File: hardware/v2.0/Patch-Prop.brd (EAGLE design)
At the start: 100 x 80 mm, 51 parts, among them IC1 TPS77033, IC2 ATMEGA168, IC3 XBEE, IC4 MMA8452Q, U1 MCP73831, U2 MCP1253, X1 USBSMD

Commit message: Tweaking naming and notes
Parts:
- removed R9: 470, SparkFun:0402-RES
- removed U1: MCP73831, SparkFun:SOT23-5
- added IC5: MCP1253, CH_Microchip:MSOP8
- added R7: 10k, rcl:R0603
- C1, C5: device rcl:C0603 -> CH_passive:0603
- C10, C9: value 4.7uF -> 0.1uF; device SparkFun:0402-CAP -> rcl:C0603
- C11: value 0.1uF -> 4.7uF
- C12: value 1uF -> .1uF; device CH_passive:0603 -> rcl:C0603
- C13: device CH_passive:0603 -> rcl:C0603
- C14: value 10uF -> .1uF; device CH_passive:0603 -> rcl:C0603
- C3: value .1uF -> 1uF
- C4: value .1uF -> 10uF; device rcl:C0603 -> CH_passive:0603
- C7: value 0.1uF -> 4.7uF; device rcl:C0603 -> SparkFun:0402-CAP
- C8: device rcl:C0603 -> SparkFun:0402-CAP
- IC2: value ATMEGA168 -> XBEE; device SparkFun:TQFP32-08 -> adafruit:XBEE
- IC3: value XBEE -> MMA8452Q; device adafruit:XBEE -> eski-ic:QFN-16
- IC4: value MMA8452Q -> ATMEGA168; device eski-ic:QFN-16 -> SparkFun:TQFP32-08
- JP2: device SparkFun-Connectors:JST-3-SMD -> SparkFun-Connectors:JST-2-SMD
- JP3: device SparkFun-Connectors:JST-2-SMD -> SparkFun-Connectors:1X02
- JP5: device SparkFun-Connectors:JST-2-SMD -> SparkFun-Connectors:JST-3-SMD
- JP7: device SparkFun-Connectors:1X02 -> SparkFun-Connectors:JST-2-SMD
- R2: value 10k -> 470; device rcl:R0603 -> SparkFun:0402-RES
- R3: value 470 -> 10k
- R4: value 10k -> 2K; device rcl:R0603 -> SparkFun:0402-RES
- R5: value 2K -> 470; device SparkFun:0402-RES -> rcl:R0603
- U2: value MCP1253 -> MCP73831; device CH_Microchip:MSOP8 -> SparkFun:SOT23-5
- moved C9 88.7 mm to (5.08, 15.2)
- moved U2 85.2 mm to (87.6, 34.3)
- moved C8 83.2 mm to (87.6, 30.5)
- moved C7 81.6 mm to (91.4, 35.6)
- moved C10 77.5 mm to (10.2, 27.9)
- moved JP3 71.5 mm to (67.3, 16.5)
- moved JP5 56.2 mm to (15.2, 77.5)
- moved C1 52.4 mm to (22.9, 33.0)
- moved JP6 48.5 mm to (19.1, 11.4)
- moved R2 44.6 mm to (87.6, 26.7)
- moved IC3 44.4 mm to (5.08, 26.7)
- moved R4 42.6 mm to (91.4, 30.5)
- moved C13 42.4 mm to (59.7, 59.7)
- moved C5 39.6 mm to (30.5, 33.0)
- moved IC4 37.8 mm to (17.8, 62.2)
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- renumbered D4 to D1, LED7 to LED1, R12 to R6, U$1 to IC6
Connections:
- net +3V3: now also C13.1, C14.1, C4.2, C9.1, IC2.1, IC3.PIN1, IC3.PIN14, IC4.18, IC4.4, IC4.6, IC5.3, IC5.7, R5.2, R7.2; no longer C13.2, C5.1, C6.1, C8.1, IC2.18, IC2.4, IC2.6, IC3.1, IC4.PIN1, IC4.PIN14, R3.2, R4.2, U2.3, U2.7
- net +5V: now also JP5.3; no longer JP2.3
- net BLUE: now also IC4.14; no longer IC2.14
- net DTR: now also C12.1; no longer C4.1
- net GND: now also C13.2, C14.2, C3.2, C4.1, C5.1, IC2.10, IC3.PIN10, IC3.PIN12, IC3.PIN5, IC3.PIN7, IC4.21, IC4.3, IC4.5, IC5.4, IC5.8, JP2.1, JP5.2, R3.1, R4.2, U2.2; no longer C1.2, C13.1, C14.1, C5.2, C6.2, IC2.21, IC2.3, IC2.5, IC3.10, IC4.PIN10, IC4.PIN12, IC4.PIN5, IC4.PIN7, JP2.2, JP6.1, R2.1, R5.2, U1.2, U2.4, U2.8
- net GREEN: now also IC4.9; no longer IC2.9
- net INT0: now also IC4.32; no longer IC2.32
- net INT1: now also IC3.PIN11, IC4.1; no longer IC2.1, IC4.PIN11
- net INT2: now also IC3.PIN9; no longer IC4.PIN9
- net MISO: now also IC4.16; no longer IC2.16
- net MOSI: now also IC4.15; no longer IC2.15
- net N$1: now also C6.1, IC2.17, SJ2.2; no longer C3.1, IC3.17, SJ1.2
- net N$10: now also C5.2, IC5.2; no longer C14.2, U2.2
- net N$11: now also R4.1, U2.5; no longer R5.1, U1.5
- net N$14: now also R2.1, U2.1; no longer R9.1, U1.1
- net N$16: now also C10.1, IC3.PIN2; no longer C7.1, IC4.PIN2
- net N$18: now also IC2.12, SJ2.1; no longer IC3.12, SJ1.1
- net N$19: now also IC2.5, SJ1.1; no longer IC3.5, SJ2.1
- net N$2: now also C6.2, R3.2; no longer C3.2, R2.2
- net N$5: now also R5.1; no longer R3.1
- net N$6: now also C1.1, IC5.5; no longer C12.1, U2.5
- net N$7: now also C1.2, IC5.6; no longer C12.2, U2.6
- net N$8: now also R2.2; no longer R9.2
- net PGOOD: now also IC5.1; no longer U2.1
- net PROXIN: now also IC4.23, JP5.1; no longer IC2.23, JP2.1
- net RED: now also IC4.13; no longer IC2.13
- net RESET: now also C12.2, IC4.29, R7.1, SJ1.2; no longer C4.2, IC2.29, R4.1, SJ2.2
- net RXD: now also IC2.2, IC4.30; no longer IC2.30, IC3.2
- net SCK: now also IC4.17; no longer IC2.17
- net SCL: now also IC3.PIN4, IC4.28; no longer IC2.28, IC4.PIN4
- net SDA: now also IC3.PIN6, IC4.27; no longer IC2.27, IC4.PIN6
- net STATUS: now also IC4.11; no longer IC2.11
- net TXD: now also IC2.3, IC4.31; no longer IC2.31, IC3.3
- net USB_VIN: now also C7.1, JP3.2, U2.4; no longer C9.1, JP6.2, U1.4
- net V+: now also C3.1, C8.1, JP2.2, JP6.1, JP7.2, U2.3; no longer C1.1, C10.1, JP3.2, JP5.2, JP7.1, U1.3
- net VIBE: now also JP6.2, JP7.1; no longer JP5.1, JP7.2
- net VIBE_CONTROL: now also IC4.12; no longer IC2.12

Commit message: Working on PCB
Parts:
- removed C7, C8: 4.7uF, SparkFun:0402-CAP
- removed JP3: (no value), SparkFun-Connectors:1X02
- added C15, C16: 4.7uF, rcl:C0603
- C1, C4, C5: device CH_passive:0603 -> rcl:C0603
- D1: value Yellow -> (none); device SparkFun:LED-0603 -> led:CHIPLED_0805
- R1: device CH_passive:0603 -> rcl:R0603
- R2: device SparkFun:0402-RES -> rcl:R0603
- R4: value 2K -> 2k; device SparkFun:0402-RES -> rcl:R0603
- moved R2 88.8 mm to (8.00, 66.0)
- moved X1 88.0 mm to (6.50, 42.0), turned to 180 degrees
- moved D1 87.5 mm to (11.0, 61.0)
- moved R4 87.0 mm to (12.0, 66.0)
- moved T2 86.6 mm to (12.0, 15.0)
- moved U2 85.3 mm to (7.00, 62.0)
- moved IC6 73.1 mm to (93.0, 14.0)
- moved JP5 68.0 mm to (83.0, 72.0), turned to 90 degrees
- moved IC5 67.8 mm to (74.0, 4.00)
- moved C1 66.8 mm to (83.0, 4.00), turned to 90 degrees
- moved L1 63.5 mm to (86.0, 4.00), turned to 90 degrees
- moved C3 62.2 mm to (59.0, 4.00), turned to 90 degrees
- moved JP1 59.6 mm to (11.0, 41.0), turned to 90 degrees
- moved R7 58.6 mm to (37.0, 30.0)
- moved C2 56.8 mm to (55.0, 4.00), turned to 90 degrees
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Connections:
- net +3V3: now also C4.1; no longer C4.2
- net GND: now also C15.2, C16.2, C4.2, C5.2; no longer C4.1, C5.1, C7.2, C8.2, JP3.1
- net N$10: now also C5.1, R1.1; no longer C5.2, R1.2
- net PGOOD: now also R1.2; no longer R1.1
- net USB_VIN: now also C16.1; no longer C7.1, JP3.2
- net V+: now also C15.1; no longer C8.1
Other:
- board size 100 x 80 mm -> 45 x 45 mm

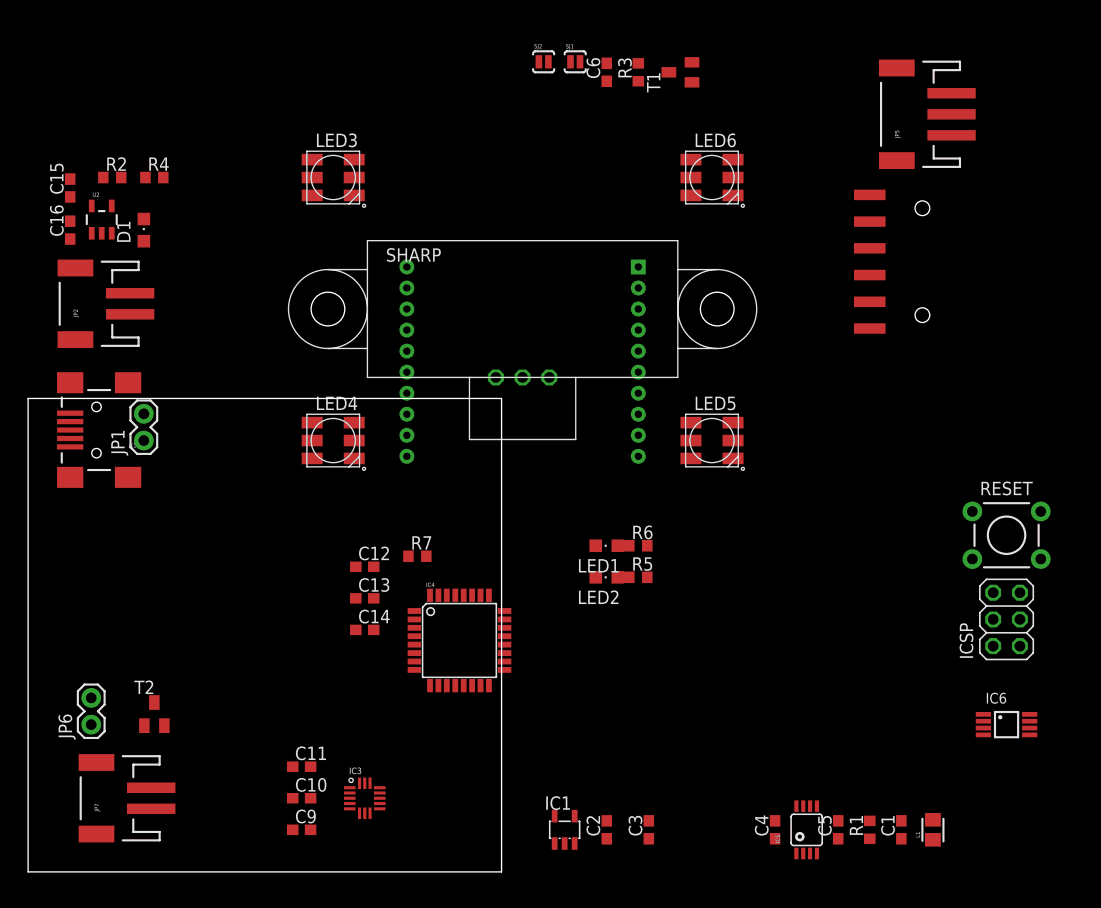
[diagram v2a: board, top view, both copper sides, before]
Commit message: Tentative part layout for propinquity board
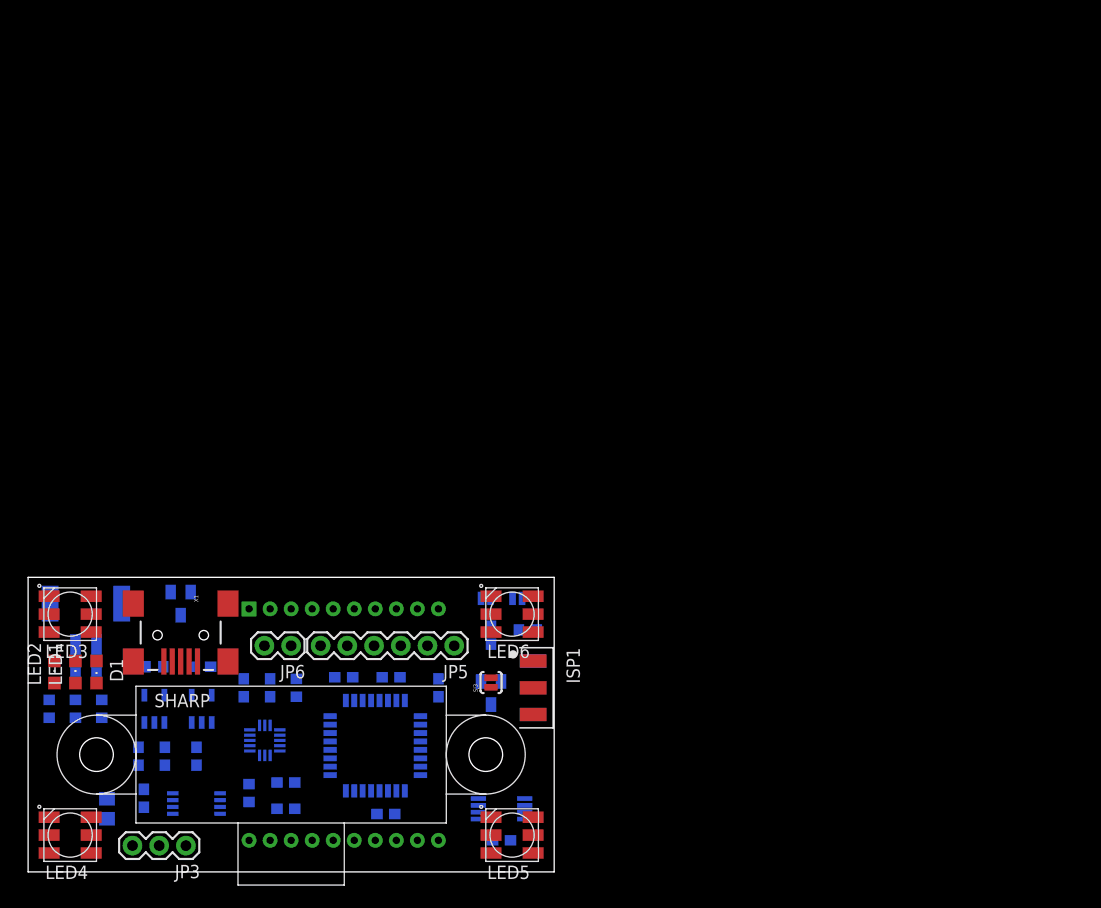
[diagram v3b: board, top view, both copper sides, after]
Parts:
- removed ICSP: (no value), pinhead:2X03
- removed JP1: (no value), SparkFun-Connectors:1X02
- removed JP4: (no value), SparkFun:1X06-SMD
- removed JP7: (no value), SparkFun-Connectors:JST-2-SMD
- removed RESET: (no value), SparkFun:TACTILE-PTH
- added C7: 4.7uF, rcl:C0603
- added ISP1: (no value), balto:2X03_BORDER
- added JP3: (no value), SparkFun-Connectors:1X03
- added SJ3: SOLDERJUMPERNO, SparkFun:SJ_2S-NO
- JP5: device SparkFun-Connectors:JST-3-SMD -> SparkFun-Connectors:1X06
- SHARP: value GP2D12TH -> GP2D12_OUTLINE; device Sparky:GP2D12 -> Sparky:GP2D12_OUTLINE
- moved L1 78.5 mm to (7.50, 6.00), flipped to the bottom, turned to 270 degrees
- moved C1 72.1 mm to (11.0, 7.00), flipped to the bottom
- moved JP5 66.0 mm to (40.5, 21.5), turned to 180 degrees
- moved T1 61.7 mm to (44.0, 17.0), flipped to the bottom, turned to 180 degrees
- moved C5 61.4 mm to (16.0, 11.0), flipped to the bottom
- moved R1 59.1 mm to (21.0, 7.50), flipped to the bottom
- moved C4 58.4 mm to (13.0, 11.0), flipped to the bottom
- moved R6 58.1 mm to (2.00, 15.5), flipped to the bottom, turned to 270 degrees
- moved IC5 58.1 mm to (16.0, 6.50), flipped to the bottom, turned to 270 degrees
- moved R5 54.9 mm to (4.50, 15.5), flipped to the bottom, turned to 270 degrees
- moved C6 54.6 mm to (44.0, 22.5), flipped to the bottom, turned to 270 degrees
- moved R3 54.0 mm to (47.5, 23.0), flipped to the bottom, turned to 0 degrees
- moved LED2 53.3 mm to (2.50, 19.0), turned to 0 degrees
- moved LED1 51.9 mm to (4.50, 19.0), turned to 0 degrees
- moved SJ1 51.7 mm to (43.5, 26.0), flipped to the bottom, turned to 180 degrees
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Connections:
- removed net INT2: IC3.PIN9
- net +3V3: now also JP5.4; no longer ICSP.2, JP4.4
- net +5V: now also JP3.3; no longer JP5.3, SHARP.VCC
- net DTR: now also JP5.1; no longer JP4.1
- net GND: now also C7.2, JP3.2, JP5.5, JP5.6, SJ3.1; no longer ICSP.6, JP1.2, JP4.5, JP4.6, JP5.2, RESET.3, RESET.4, SHARP.GND
- net INT0: now also IC3.PIN11
- net INT1: now also IC3.PIN9; no longer IC3.PIN11
- net MISO: now also ISP1.1; no longer ICSP.1
- net MOSI: no longer ICSP.4
- net PROXIN: now also JP3.1; no longer JP5.1, SHARP.VOUT
- net RESET: now also ISP1.5, SJ3.2; no longer ICSP.5, RESET.1, RESET.2
- net RXD: now also JP5.3; no longer JP4.3
- net SCK: now also ISP1.3; no longer ICSP.3
- net TXD: now also JP5.2; no longer JP4.2
- net V+: now also C7.1; no longer JP1.1, JP7.2
- net VIBE: no longer JP7.1
- net VIBE_CONTROL: now also IC4.2; no longer IC4.12
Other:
- board size 45 x 45 mm -> 50 x 28 mm

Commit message: All routed except for LEDs (which will be hard)
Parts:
- removed LED2: (no value), led:CHIPLED_0805
- removed R6: 470, rcl:R0603
- added R8, R9: 4.7k, rcl:R0603
- moved SJ2 22.1 mm to (38.2, 5.50), turned to 90 degrees
- moved R7 13.0 mm to (38.5, 17.5)
- moved C10 10.7 mm to (15.0, 11.0), turned to 270 degrees
- moved SJ3 8.06 mm to (48.0, 11.0), flipped to the bottom, turned to 0 degrees
- moved C1 7.07 mm to (4.00, 6.00)
- moved C11 6.96 mm to (18.0, 11.0), turned to 270 degrees
- moved C4 4.47 mm to (11.0, 7.00)
- moved C2 4.35 mm to (8.80, 7.00)
- moved C5 4.00 mm to (12.0, 11.0)
- moved L1 3.91 mm to (5.00, 3.00), turned to 180 degrees
- moved C3 3.35 mm to (20.0, 16.0), turned to 180 degrees
- moved C6 3.08 mm to (45.8, 25.0), turned to 90 degrees
- moved R5 2.42 mm to (2.10, 15.8)
- moved LED1 2.24 mm to (2.50, 18.0)
- moved R3 2.24 mm to (48.5, 25.0), turned to 270 degrees
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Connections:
- removed net N$4: LED2.A, R6.1
- net +3V3: now also ISP1.2, R8.2, R9.2
- net GND: now also ISP1.6; no longer LED2.C
- net GREEN: now also IC4.13; no longer IC4.9
- net MOSI: now also ISP1.4
- net RED: now also IC4.9; no longer IC4.13
- net SCL: now also R9.1
- net SDA: now also R8.1
- net STATUS: no longer R6.2
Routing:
- net GND: track 0.00 -> 204.4 mm, vias 0 -> 7
- net +3V3: track 0.00 -> 132.5 mm, vias 0 -> 4
- net V+: track 0.00 -> 81.3 mm, vias 0 -> 5
- net RESET: track 0.00 -> 43.8 mm, vias 0 -> 4
- net N$1: track 0.00 -> 38.3 mm, vias 0 -> 2
- net TXD: track 0.00 -> 35.8 mm, vias 0 -> 1
- net VIBE_CONTROL: track 0.00 -> 32.0 mm, vias 0 -> 2
- net N$10: track 0.00 -> 27.5 mm, vias 0 -> 2
- net USB_VIN: track 0.00 -> 26.2 mm, vias 0 -> 2
- net RXD: track 0.00 -> 26.1 mm
- net MISO: track 0.00 -> 20.2 mm, vias 0 -> 1
- net MOSI: track 0.00 -> 19.6 mm, vias 0 -> 2
- net SCK: track 0.00 -> 19.5 mm, vias 0 -> 1
- net PROXIN: track 0.00 -> 18.7 mm
- net N$19: track 0.00 -> 15.8 mm, vias 0 -> 1
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
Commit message: Tweaks, still 4 drc errors
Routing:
- net VIBE_CONTROL: track 32.0 -> 30.5 mm
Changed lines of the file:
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@@
 </class>
 </classes>
-<designrules name="default">
-<description language="de">&lt;b&gt;EAGLE Design Rules&lt;/b&gt;
-&lt;p&gt;
-Die Standard-Design-Rules sind so gewählt, dass sie für
-die meisten Anwendungen passen. Sollte ihre Platine
-besondere Anforderungen haben, treffen Sie die erforderlichen
-Einstellungen hier und speichern die Design Rules unter
-einem neuen Namen ab.</description>
+<designrules name="APC">
 <description language="en">&lt;b&gt;EAGLE Design Rules&lt;/b&gt;
 &lt;p&gt;
@@
 <param name="mtCopper" value="0.035mm 0.035mm 0.035mm 0.035mm 0.035mm 0.035mm 0.035mm 0.035mm 0.035mm 0.035mm 0.035mm 0.035mm 0.035mm 0.035mm 0.035mm 0.035mm"/>
 <param name="mtIsolate" value="1.5mm 0.15mm 0.2mm 0.15mm 0.2mm 0.15mm 0.2mm 0.15mm 0.2mm 0.15mm 0.2mm 0.15mm 0.2mm 0.15mm 0.2mm"/>
-<param name="mdWireWire" value="8mil"/>
-<param name="mdWirePad" value="8mil"/>
-<param name="mdWireVia" value="8mil"/>
-<param name="mdPadPad" value="8mil"/>
-<param name="mdPadVia" value="8mil"/>
-<param name="mdViaVia" value="8mil"/>
-<param name="mdSmdPad" value="8mil"/>
-<param name="mdSmdVia" value="8mil"/>
-<param name="mdSmdSmd" value="8mil"/>
+<param name="mdWireWire" value="7mil"/>
+<param name="mdWirePad" value="7mil"/>
+<param name="mdWireVia" value="7mil"/>
+<param name="mdPadPad" value="7mil"/>
+<param name="mdPadVia" value="7mil"/>
+<param name="mdViaVia" value="7mil"/>
+<param name="mdSmdPad" value="1mil"/>
+<param name="mdSmdVia" value="1mil"/>
+<param name="mdSmdSmd" value="1mil"/>
 <param name="mdViaViaSameLayer" value="8mil"/>
 <param name="mnLayersViaInSmd" value="2"/>
-<param name="mdCopperDimension" value="40mil"/>
+<param name="mdCopperDimension" value="8mil"/>
 <param name="mdDrill" value="8mil"/>
 <param name="mdSmdStop" value="0mil"/>
-<param name="msWidth" value="10mil"/>
-<param name="msDrill" value="24mil"/>
-<param name="msMicroVia" value="9.99mm"/>
+<param name="msWidth" value="7mil"/>
+<param name="msDrill" value="15mil"/>
+<param name="msMicroVia" value="10mm"/>
 <param name="msBlindViaRatio" value="0.5"/>
 <param name="rvPadTop" value="0.25"/>
@@
 <param name="rvMicroViaOuter" value="0.25"/>
 <param name="rvMicroViaInner" value="0.25"/>
-<param name="rlMinPadTop" value="10mil"/>
+<param name="rlMinPadTop" value="12mil"/>
 <param name="rlMaxPadTop" value="20mil"/>
 <param name="rlMinPadInner" value="10mil"/>
 <param name="rlMaxPadInner" value="20mil"/>
-<param name="rlMinPadBottom" value="10mil"/>
+<param name="rlMinPadBottom" value="12mil"/>
 <param name="rlMaxPadBottom" value="20mil"/>
-<param name="rlMinViaOuter" value="8mil"/>
+<param name="rlMinViaOuter" value="10mil"/>
 <param name="rlMaxViaOuter" value="20mil"/>
-<param name="rlMinViaInner" value="8mil"/>
+<param name="rlMinViaInner" value="10mil"/>
 <param name="rlMaxViaInner" value="20mil"/>
 <param name="rlMinMicroViaOuter" value="4mil"/>
@@
 <param name="mlMinCreamFrame" value="0mil"/>
 <param name="mlMaxCreamFrame" value="0mil"/>
-<param name="mlViaStopLimit" value="0mil"/>
+<param name="mlViaStopLimit" value="25mil"/>
 <param name="srRoundness" value="0"/>
 <param name="srMinRoundness" value="0mil"/>
@@
 <param name="dpGapFactor" value="2.5"/>
 <param name="checkGrid" value="0"/>
-<param name="checkAngle" value="0"/>
+<param name="checkAngle" value="1"/>
 <param name="checkFont" value="1"/>
 <param name="checkRestrict" value="1"/>
@@
 <wire x1="23.7" y1="19.15" x2="23.7" y2="16.3" width="0.3048" layer="16"/>
 <wire x1="23.7" y1="16.3" x2="22.9" y2="15.5" width="0.3048" layer="16"/>
-<wire x1="22.9" y1="15.5" x2="22.4" y2="15.5" width="0.3048" layer="16"/>
-<wire x1="22.4" y1="15.5" x2="21" y2="14.1" width="0.3048" layer="16"/>
+<wire x1="22.9" y1="15.5" x2="22.3" y2="15.5" width="0.3048" layer="16"/>
+<wire x1="22.3" y1="15.5" x2="20.9" y2="14.1" width="0.3048" layer="16"/>
 <wire x1="22.9" y1="6.4" x2="19.8" y2="9.5" width="0.3048" layer="1"/>
 <via x="19.8" y="9.5" extent="1-16" drill="0.5" diameter="0.4064" shape="octagon"/>
@@
 <wire x1="19.2" y1="10.5" x2="19.2" y2="11.5" width="0.3048" layer="16"/>
 <wire x1="19.3" y1="10.6" x2="19.2" y2="10.5" width="0.3048" layer="16"/>
-<wire x1="19.2" y1="14.1" x2="21" y2="14.1" width="0.3048" layer="16"/>
-<wire x1="21.6" y1="12.525" x2="21.6" y2="13.5" width="0.3048" layer="16"/>
-<wire x1="21.6" y1="13.5" x2="21" y2="14.1" width="0.3048" layer="16"/>
+<wire x1="19.2" y1="14.1" x2="20.9" y2="14.1" width="0.3048" layer="16"/>
+<wire x1="21.6" y1="12.525" x2="21.6" y2="13.4" width="0.3048" layer="16"/>
+<wire x1="21.6" y1="13.4" x2="20.9" y2="14.1" width="0.3048" layer="16"/>
 <contactref element="ISP1" pad="2"/>
 <wire x1="27" y1="6.9" x2="30.3" y2="10.2" width="0.3048" layer="1"/>
@@
 <via x="20.3" y="22.8" extent="1-16" drill="0.5" shape="octagon"/>
 <wire x1="20.3" y1="22.8" x2="20.6" y2="23.1" width="0.3048" layer="1"/>
-<wire x1="32.9" y1="18.6" x2="32.9" y2="13.7" width="0.3048" layer="1"/>
-<wire x1="32.9" y1="18.6" x2="30.4" y2="18.6" width="0.3048" layer="1"/>
-<wire x1="30.4" y1="18.6" x2="29.1" y2="19.9" width="0.3048" layer="1"/>
 <wire x1="29.1" y1="19.9" x2="29.1" y2="22.7" width="0.3048" layer="1"/>
 <wire x1="29.1" y1="22.7" x2="28.4" y2="23.4" width="0.3048" layer="1"/>
 <wire x1="28.4" y1="23.4" x2="20.9" y2="23.4" width="0.3048" layer="1"/>
 <wire x1="20.9" y1="23.4" x2="20.3" y2="22.8" width="0.3048" layer="1"/>
+<wire x1="29.1" y1="19.9" x2="32.9" y2="16.1" width="0.3048" layer="1"/>
+<wire x1="32.9" y1="16.1" x2="32.9" y2="13.7" width="0.3048" layer="1"/>
 </signal>
 <signal name="VIBE">
@@
 <contactref element="R9" pad="1"/>
 <wire x1="28.7074" y1="11.6" x2="27.4" y2="11.6" width="0.3048" layer="16"/>
-<wire x1="23.1" y1="13.9" x2="23.1" y2="12.525" width="0.3048" layer="16"/>
+<wire x1="23.1" y1="13.8" x2="23.1" y2="12.525" width="0.3048" layer="16"/>
 <wire x1="27.4" y1="11.6" x2="26.4" y2="12.6" width="0.3048" layer="16"/>
 <wire x1="26.4" y1="12.6" x2="26.4" y2="13.7" width="0.3048" layer="16"/>
 <wire x1="26.4" y1="13.7" x2="25.8" y2="14.3" width="0.3048" layer="16"/>
 <wire x1="25.8" y1="14.3" x2="25" y2="14.3" width="0.3048" layer="16"/>
-<wire x1="25" y1="14.3" x2="23.5" y2="14.3" width="0.3048" layer="16"/>
-<wire x1="23.5" y1="14.3" x2="23.1" y2="13.9" width="0.3048" layer="16"/>
+<wire x1="25" y1="14.3" x2="23.6" y2="14.3" width="0.3048" layer="16"/>
+<wire x1="23.6" y1="14.3" x2="23.1" y2="13.8" width="0.3048" layer="16"/>
 <wire x1="25" y1="16.15" x2="25" y2="14.3" width="0.3048" layer="16"/>
 </signal>
